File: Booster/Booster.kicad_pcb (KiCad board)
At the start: 2 copper layers, 97 x 60 mm, 120 parts, among them IC401 SN754410, J101 Track, J301 15VDC, J601 StatusLED, J701 Conn_01x04, P201 CONN_01X02, P202 CONN_01X02, P601 ~OVERCURRENT_OUT, P602 ~OVERCURRENT_OUT_OP, P603 MSTR_SW, P604 MSTR_SW_OUT, P605 MSTR_SW_OUT_OP, P606 ~DRIVER_ENABLE_OUT_OP, P607 ~DRIVER_ENABLE_OUT, P701 REVERSER_OUT, P702 REVERSER_OUT_OP, Q601 BC807-40, Q602 BC807-40, Q603 BC807-40, Q604 BC817-40, Q701 BC817-40, SW601 DIP, U201 6N137, U203 LM339, U301 LM7805_TO220, U501 LM338, U502 LM358, U503 NE555, U504 74HC08, U602 PC817, U603 PC817, U604 PC817, U701 74HC86, U702 PC817

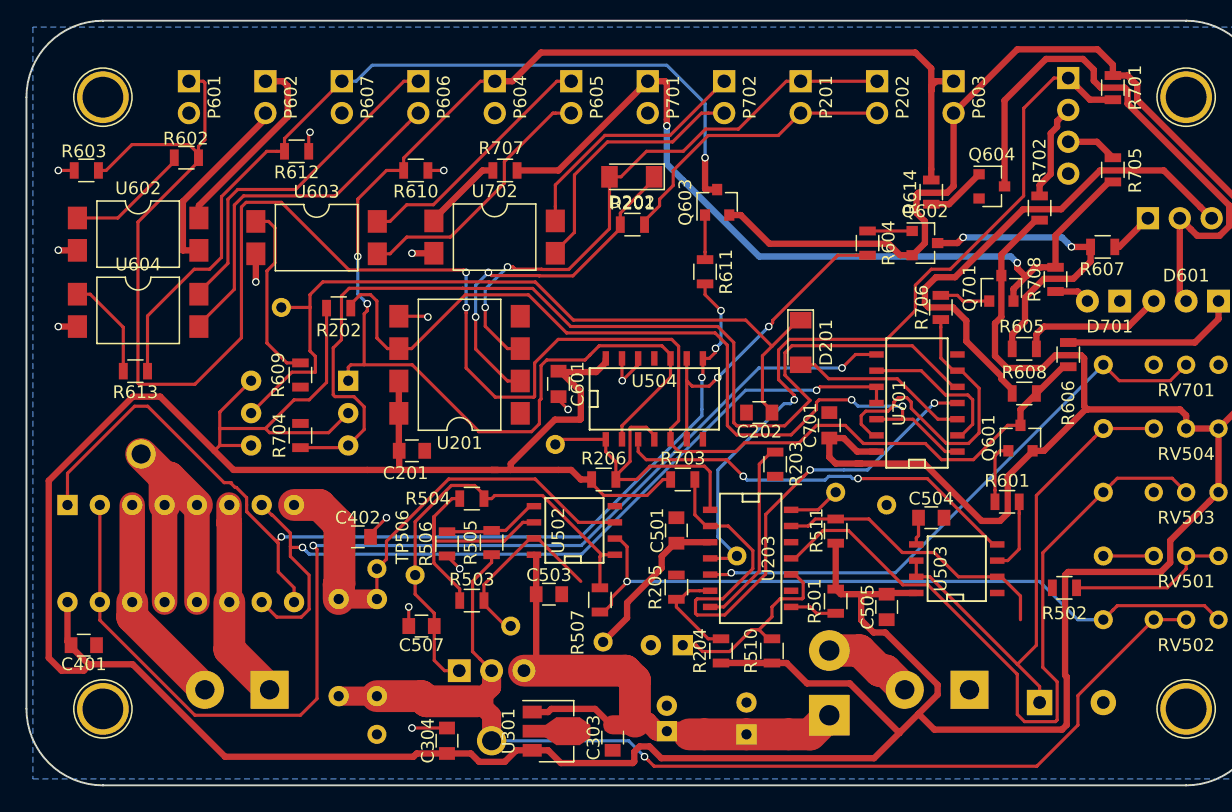
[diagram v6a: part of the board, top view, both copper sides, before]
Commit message: More ground connections and other traces added. Still need to reposition R609.
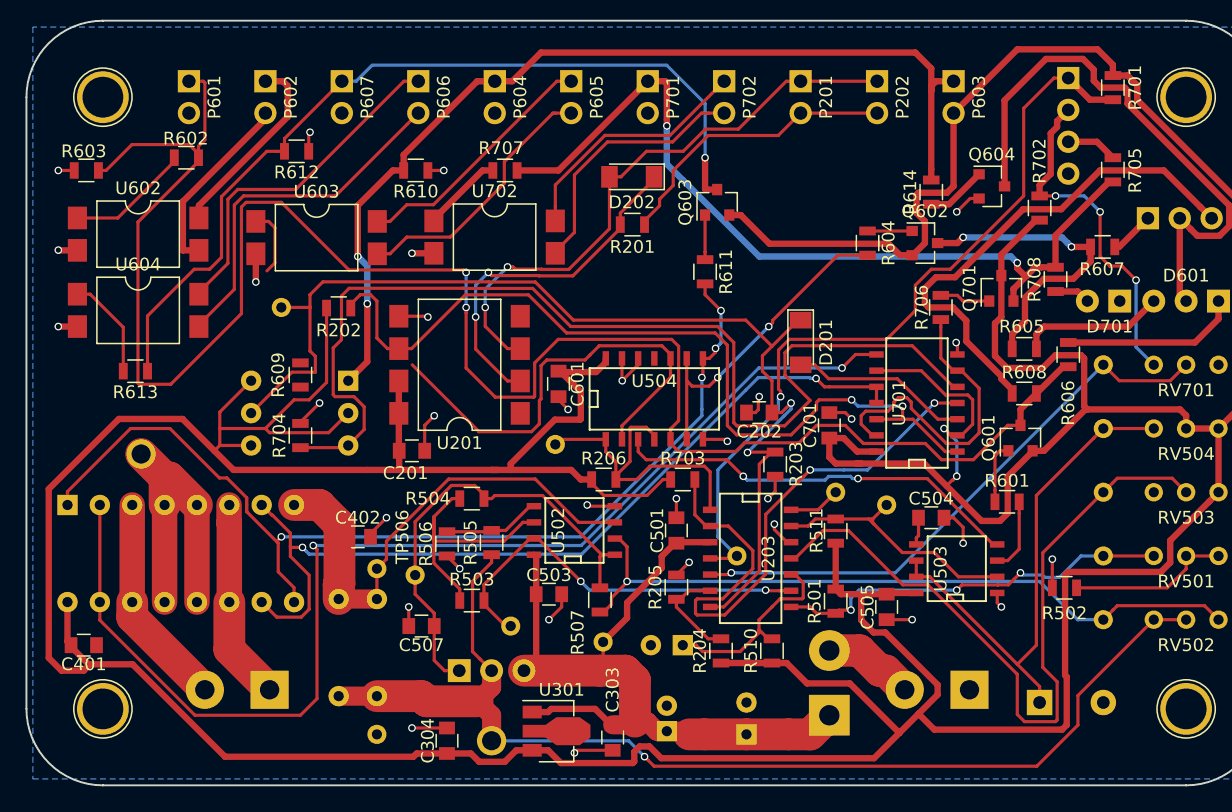
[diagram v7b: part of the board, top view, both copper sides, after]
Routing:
- net GND: track 49.7 -> 87.5 mm, vias 14 -> 32
- net Net-(R501-Pad1): track 7.67 -> 31.4 mm, vias 0 -> 3
- net /Reversing/IR_Led: track 7.68 -> 27.3 mm, vias 0 -> 3
- net Net-(R503-Pad2): track 15.2 -> 32.0 mm, vias 0 -> 2
- net Net-(C202-Pad1): track 77.6 -> 86.9 mm, vias 0 -> 2
- net Net-(R609-Pad1): track 14.3 -> 5.35 mm
- net /Overcurrent Detector/MSTR_SW: track 118.5 -> 113.3 mm
- net +5V: track 452.3 -> 457.1 mm, vias 0 -> 2
- net +15V: track 59.8 -> 62.2 mm
- net Net-(R511-Pad1): track 22.6 -> 20.6 mm
- net /Reversing/PhotoDiode: track 63.2 -> 62.0 mm
- net /Status/STATUS_GREEN_LED: track 150.1 -> 149.0 mm
- net /Driver/DRIVER_SIGNAL: track 67.2 -> 67.8 mm

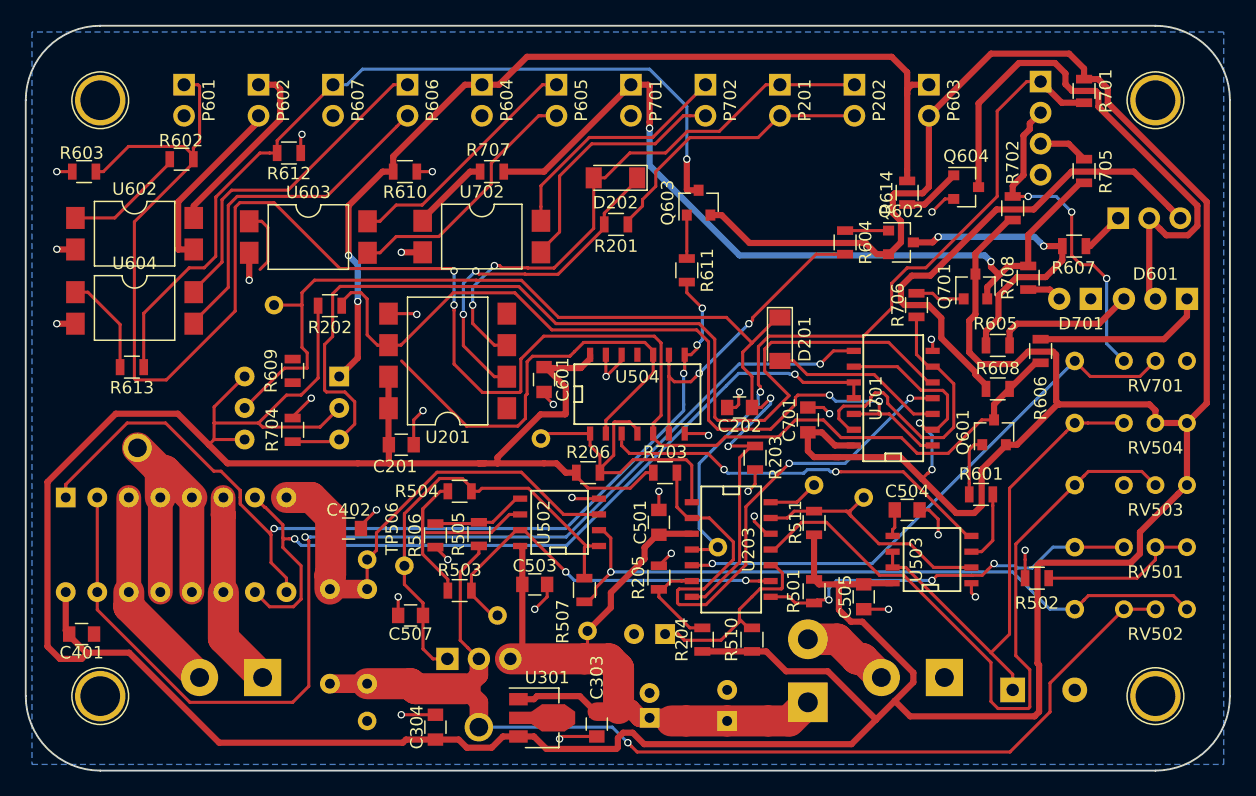
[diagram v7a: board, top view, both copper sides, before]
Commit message: Further trace optimizations and fixed a few missing connections.
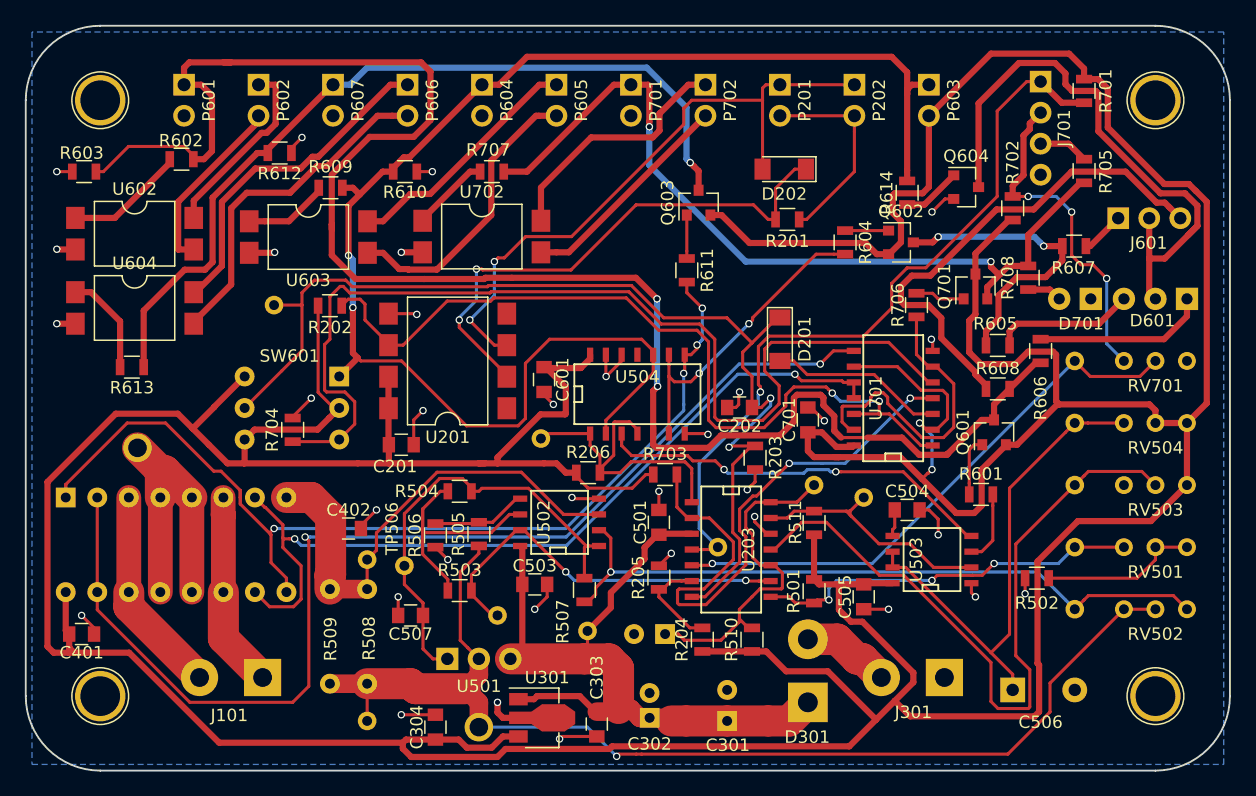
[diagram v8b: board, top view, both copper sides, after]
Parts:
- moved R609 15.1 mm to (124.5, 93.0), turned to 0 degrees
- moved R201 13.8 mm to (161.3, 95.6)
- moved D202 13.6 mm to (161.1, 91.5)
- moved R612 0.75 mm to (120.5, 90.2)
- moved R703 0.15 mm to (151.5, 116.2)
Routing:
- net Net-(D202-Pad1): track 28.1 -> 43.2 mm
- net GND: track 87.5 -> 96.7 mm, vias 32 -> 34
- net Net-(C502-Pad1): track 20.0 -> 27.9 mm
- net /Status/STATUS_GREEN_LED: track 149.0 -> 142.2 mm
- net /DCC Input/DCC_GND_Input: track 23.0 -> 16.5 mm
- net /Overcurrent Detector/MSTR_SW: track 113.3 -> 118.5 mm
- net /DCC Input/DCC_Input: track 46.4 -> 51.2 mm
- net Net-(P605-Pad2): track 20.8 -> 24.9 mm
- net Net-(R505-Pad1): track 89.3 -> 92.6 mm
- net Net-(P702-Pad2): track 20.5 -> 17.8 mm
- net Net-(D601-Pad2): track 44.7 -> 47.1 mm
- net +5V: track 457.1 -> 459.4 mm
- net Net-(R609-Pad1): track 5.35 -> 6.89 mm
- net /DCC Input/DCC: track 68.1 -> 66.9 mm
- net Net-(C202-Pad1): track 86.9 -> 86.0 mm
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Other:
- net class Default: clearance 0.254 -> 0.25; trace_width 0.254 -> 0.25
- net class HighAmp removed
- rule trace_clearance: 0.254 -> 0.25
